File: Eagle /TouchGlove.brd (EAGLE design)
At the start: 69.5 x 25.3 mm, 77 parts, among them Q1 SI2302CDS 2.9A/20V, Q2 SI2302CDS 2.9A/20V, Q3 SI2302CDS 2.9A/20V, Q4 SI2302CDS 2.9A/20V, Q5 SI2302CDS 2.9A/20V, SW1 300mA/4V, Y1 16 MHz

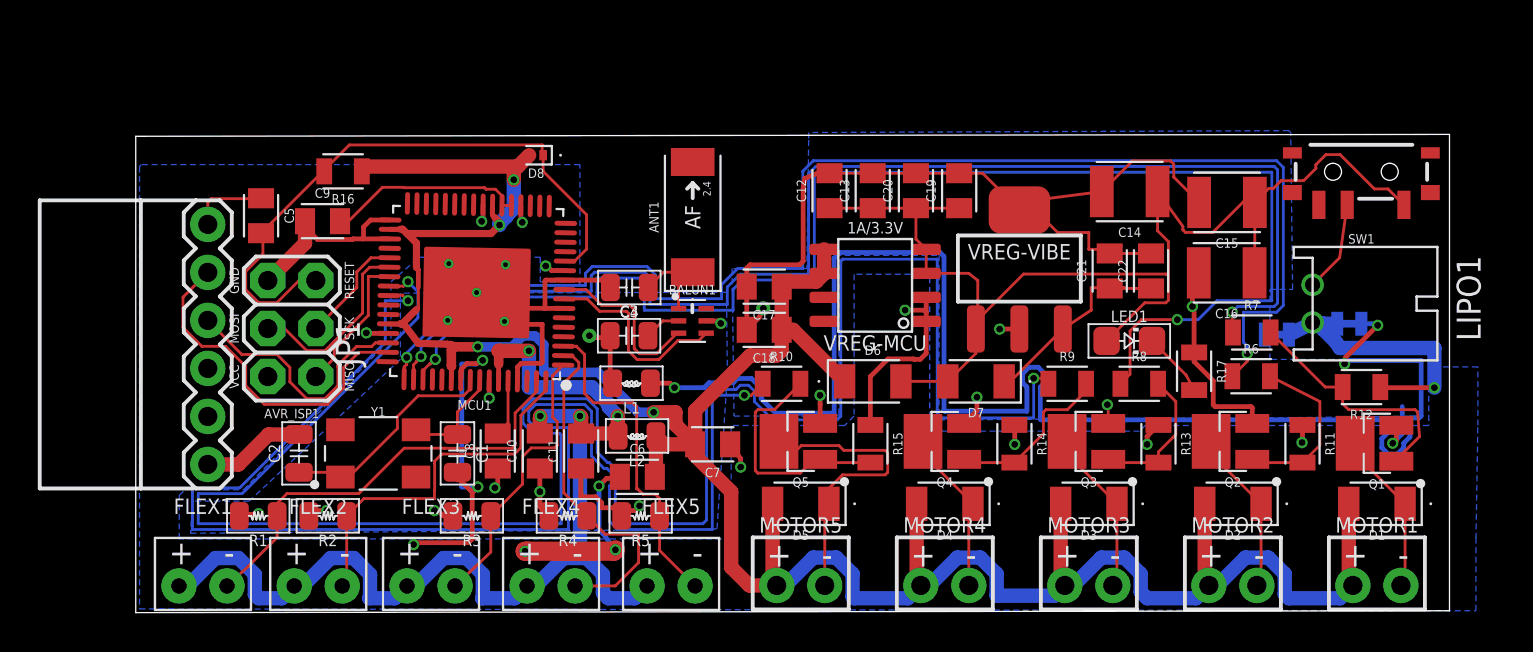
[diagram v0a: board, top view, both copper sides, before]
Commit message: Fixing DRC errors in touchglove brd
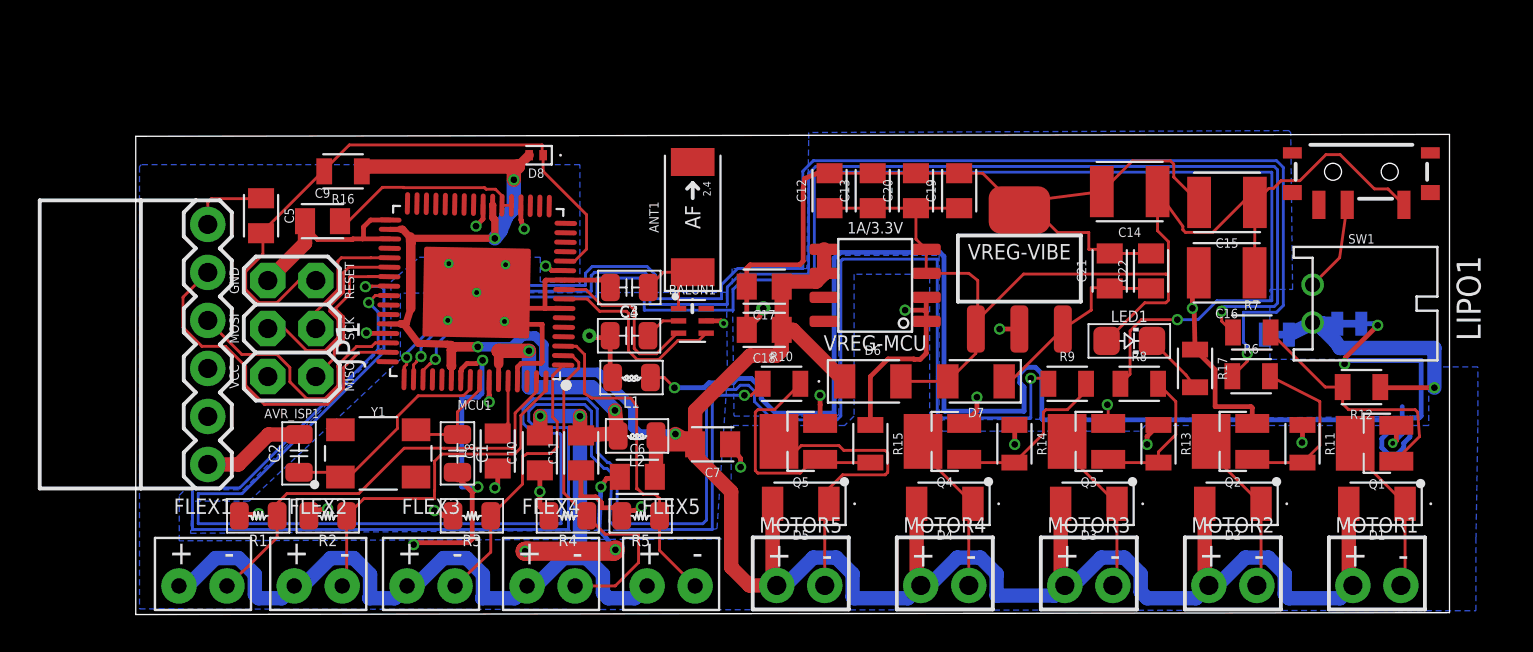
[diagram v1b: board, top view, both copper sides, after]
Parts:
- moved L1 0.30 mm to (34.2, 13.5)
- moved R17 0.16 mm to (64.0, 14.0)
- moved C10 0.10 mm to (29.4, 9.55)
- moved C11 0.10 mm to (31.6, 9.55)
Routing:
- net MISO: track 7.87 -> 9.90 mm
- net VCC: track 144.1 -> 145.4 mm
- net MOSI: track 9.94 -> 10.9 mm
- net PINKY-VIBE: track 73.8 -> 72.8 mm
- net SCK: track 5.93 -> 6.85 mm
- net INDEX-VIBE: track 70.1 -> 71.0 mm
- net AGND: track 37.3 -> 38.2 mm
- net GND: track 77.9 -> 78.6 mm
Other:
- board size 69.5 x 25.3 mm -> 69.5 x 25.4 mm

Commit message: Rotated that shitty chip.
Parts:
- removed D6: 1A/50V, PiB_discrete_semiconductors:SODFL3516X170
- removed MOTOR1, MOTOR2, MOTOR3, MOTOR4, MOTOR5: (no value), PiB:CONNECTOR_MOTOR
- added VIBE1, VIBE2, VIBE3, VIBE4, VIBE5: Molex VERT 1.25mm pitch, PiB_actuators:_MOLEX-0530470210_VERT_PITCH-1.25MM
- FLEX1, FLEX2, FLEX3, FLEX4, FLEX5: device PiB:CONNECTOR_FSR -> PiB_sensors:_MOLEX-0530470210_VERT_PITCH-1.25MM
- VREG-MCU: device PiB_ic_power:SOIC-8_W3.9MM -> PiB_ic_power:SOIC127P600X265-8
- moved D8 14.6 mm to (14.6, 24.6)
- moved SUPPLY39 3.77 mm to (70.0, 13.3), turned to 270 degrees
- moved SUPPLY38 3.16 mm to (68.0, 12.7), turned to 90 degrees
- moved R16 1.23 mm to (17.8, 24.0)
- moved FLEX2 1.20 mm to (17.7, 2.58)
- moved FLEX3 1.20 mm to (23.6, 2.58)
- moved FLEX4 1.20 mm to (30.0, 2.58)
- moved FLEX5 1.20 mm to (36.3, 2.58)
- moved FLEX1 1.15 mm to (11.6, 2.63)
- moved D1 0.76 mm to (73.6, 6.11)
- moved D2 0.75 mm to (66.1, 6.11)
- moved D3 0.75 mm to (58.4, 6.11)
- moved D4 0.75 mm to (50.8, 6.11)
- moved D5 0.75 mm to (43.2, 6.11)
- turned MCU1 to 180 degrees
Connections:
- net AVCC: now also FLEX1.1, FLEX2.1, FLEX3.1, FLEX4.1, FLEX5.1; no longer FLEX1.+, FLEX2.+, FLEX3.+, FLEX4.+, FLEX5.+
- net FLEX-INDEX: now also FLEX2.2; no longer FLEX2.-
- net FLEX-MIDDLE: now also FLEX3.2; no longer FLEX3.-
- net FLEX-PINKY: now also FLEX5.2; no longer FLEX5.-
- net FLEX-RING: now also FLEX4.2; no longer FLEX4.-
- net FLEX-THUMB: now also FLEX1.2; no longer FLEX1.-
- net GND: now also C12.2, C13.2, C14.2, C15.2, C16.2, C17.2, C18.2, R17.1
- net N$1: now also VIBE1.2; no longer MOTOR1.-
- net N$2: now also VIBE2.2; no longer MOTOR2.-
- net N$24: no longer D6.K
- net N$3: now also VIBE3.2; no longer MOTOR3.-
- net N$4: now also VIBE4.2; no longer MOTOR4.-
- net N$5: now also VIBE5.2; no longer MOTOR5.-
- net NGND: no longer C12.2, C13.2, C14.2, C15.2, C16.2, C17.2, C18.2, R17.1
- net VCC: now also VIBE1.1, VIBE2.1, VIBE3.1, VIBE4.1, VIBE5.1; no longer D6.A, MOTOR1.+, MOTOR2.+, MOTOR3.+, MOTOR4.+, MOTOR5.+
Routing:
- net NGND: track 65.4 -> 19.6 mm, vias 7 -> 13
- net N$19: track 78.8 -> 54.4 mm, vias 3 -> 1
- net GND: track 78.6 -> 66.7 mm, vias 16 -> 25
- net VCC: track 145.4 -> 135.1 mm
- net N$5: track 16.5 -> 11.5 mm
- net RING-VIBE: track 107.7 -> 102.9 mm
- net FLEX-RING: track 18.4 -> 14.9 mm
- net RESET: track 32.7 -> 36.1 mm
- net AVCC: track 60.5 -> 57.3 mm, vias 4 -> 5
- net N$22: track 12.8 -> 9.65 mm
- net N$16: track 13.3 -> 16.3 mm
- net N$24: track 64.1 -> 61.9 mm
- net MISO: track 9.90 -> 7.85 mm
- net N$14: track 9.30 -> 10.8 mm
- net N$4: track 8.80 -> 10.3 mm
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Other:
- board size 69.5 x 25.4 mm -> 69.5 x 25.3 mm

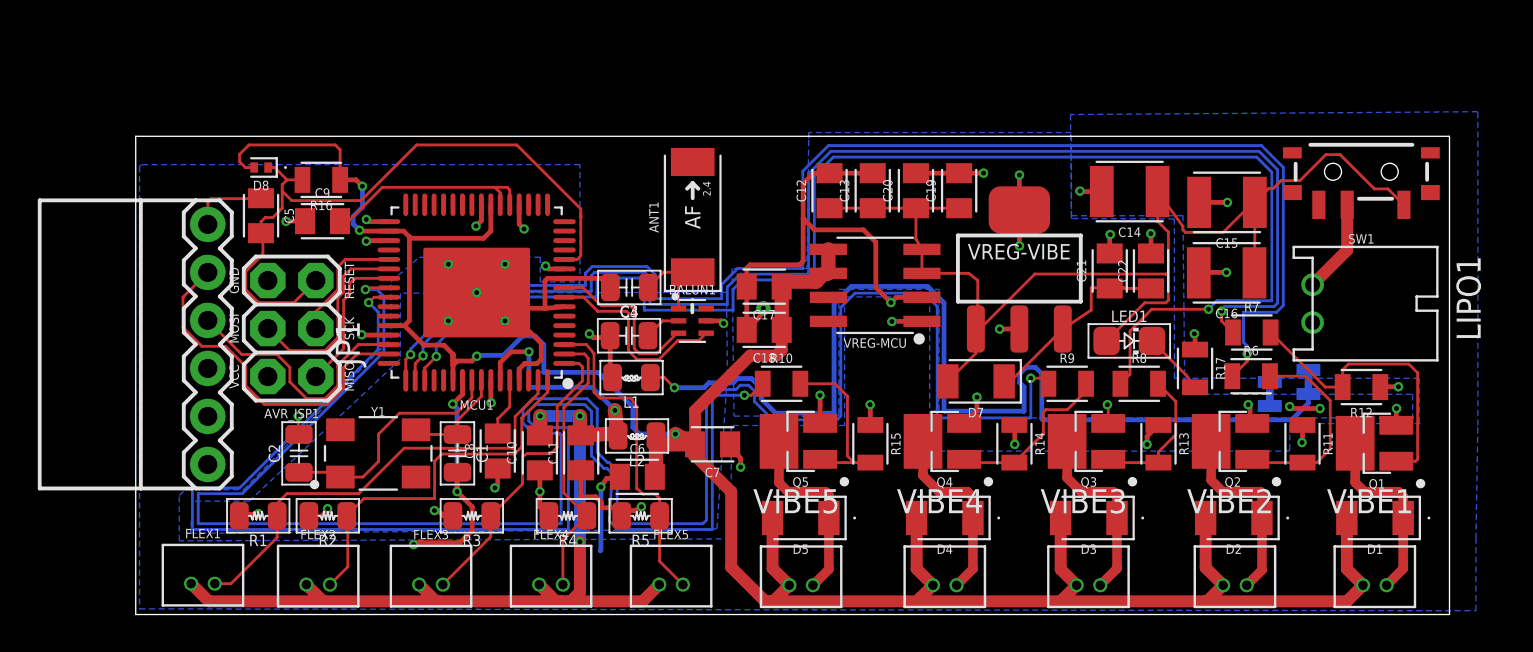
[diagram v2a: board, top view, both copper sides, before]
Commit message: Fixing very large amount of bugs in touch glove schematic
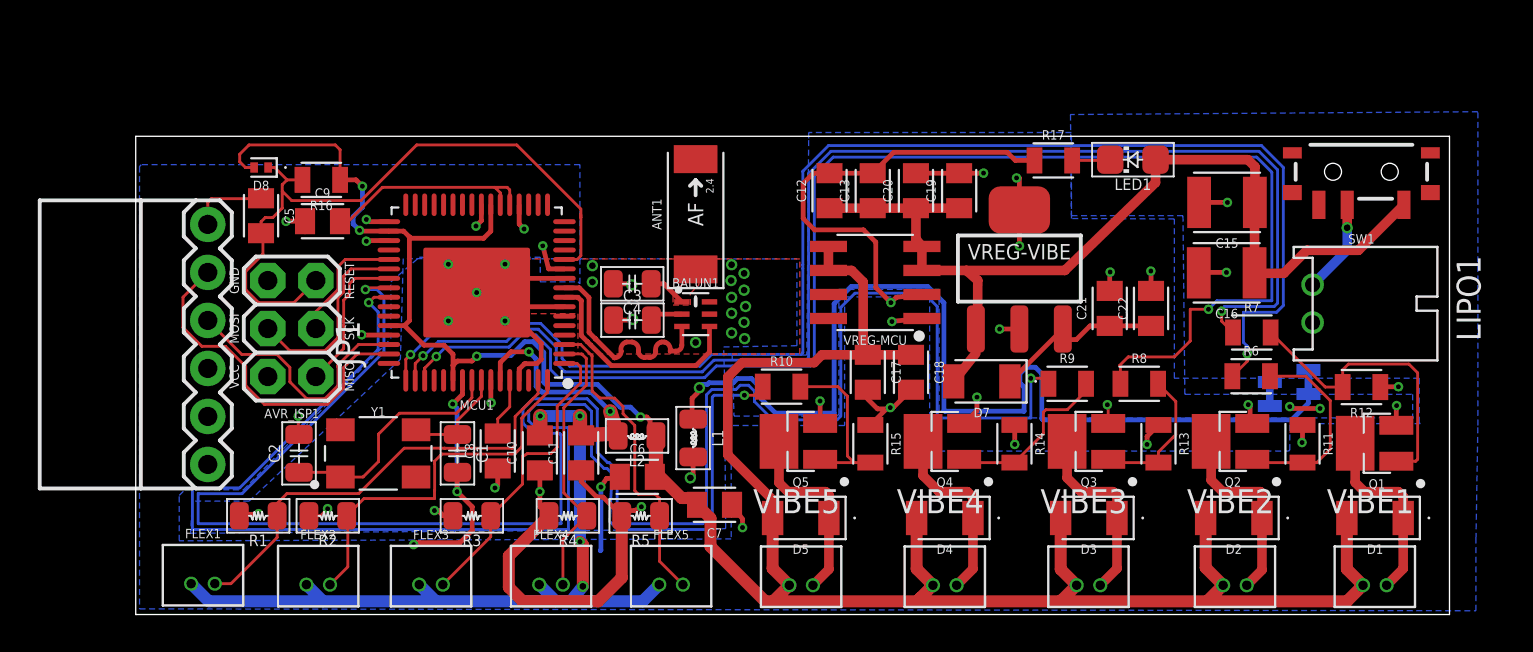
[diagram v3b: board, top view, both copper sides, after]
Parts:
- removed C14: 100uF/10V, PiB_capacitors:CAPC3225X270_SMD-1210
- moved R17 13.3 mm to (56.5, 25.0), turned to 0 degrees
- moved LED1 9.59 mm to (60.8, 25.1), turned to 180 degrees
- moved C18 8.08 mm to (49.0, 13.8), turned to 270 degrees
- moved C17 7.11 mm to (46.7, 13.8), turned to 270 degrees
- moved L1 4.57 mm to (37.5, 10.3), turned to 270 degrees
- moved C7 3.20 mm to (38.6, 6.80)
- moved C21 1.98 mm to (59.5, 17.2)
- moved C22 1.98 mm to (61.7, 17.2)
- moved C3 0.85 mm to (34.3, 16.6)
- moved BALUN1 0.40 mm to (37.6, 16.9)
- moved D7 0.30 mm to (52.8, 13.3)
- moved C4 0.25 mm to (34.3, 18.5)
- moved ANT1 0.22 mm to (37.6, 22.2)
- moved R10 0.15 mm to (42.2, 13.1)
- moved VREG-MCU 0.15 mm to (47.1, 18.6)
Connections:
- removed net N$24: C12.1, C13.1, C14.1, C15.1, C16.1, C19.1, C20.1, D7.K, LED1.A, SW1.1, VREG-MCU.3, VREG-MCU.4, VREG-VIBE.1
- new net VBAT: C12.1, C13.1, C15.1, C16.1, C19.1, C20.1, D7.K, LED1.A, SW1.1, VREG-MCU.3, VREG-MCU.4, VREG-VIBE.1
- net GND: no longer C14.2
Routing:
- net N$24: track 61.9 -> 0.00 mm
- net VBAT: track 0.00 -> 54.6 mm
- net AGND: track 37.8 -> 46.3 mm, vias 9 -> 23
- net VCC: track 135.1 -> 139.8 mm
- net N$9: track 4.92 -> 2.02 mm
- net 3.3V: track 11.9 -> 9.23 mm
- net N$10: track 9.13 -> 11.5 mm
- net GND: track 66.7 -> 68.3 mm, vias 25 -> 22
- net N$25: track 3.35 -> 2.03 mm
- net N$11: track 10.6 -> 11.9 mm
- net N$19: track 54.4 -> 53.4 mm
- net AVCC: track 57.3 -> 56.4 mm, vias 5 -> 6
- net FLEX-PINKY: track 17.3 -> 16.8 mm
- net N$15: vias 0 -> 1
- added copper zone on layer 1, net AGND
- added copper zone on layer 1, net N$9

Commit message: Rev 1: Ready for fab.
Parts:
- added U$1: (no value), PiB_logo:PIB_LOGO_10MM
- C1, C2: device PiB_capacitors:_CER_SMD-805 -> PiB_capacitors:CAPC2012X95_SMD-0805
- C3: value 22PF/250V -> 22pF/250V; device PiB_capacitors:_CER_SMD-805 -> PiB_capacitors:CAPC2012X95_SMD-0805
- C4: value 0.75PF/100V -> 0.75pF/100V; device PiB_capacitors:_CER_SMD-805 -> PiB_capacitors:CAPC2012X95_SMD-0805
- L1, L2: device PiB_inductors:_SMD-805 -> PiB_inductors:INDC2012X145
- LED1: device PiB_leds:LED_SMD-805_ -> PiB_leds:LEDC2012X120_LED-0805
- R1, R2, R3, R4, R5: device PiB_resistors:RESISTOR_SMD-805 -> PiB_resistors:RESC2012X60_SMD-0805
- VREG-VIBE: device PiB_ic_power:SOT223-4 -> PiB_ic_power:SOT229P700X180-4
- moved C7 0.30 mm to (38.3, 6.80)
- moved R13 0.25 mm to (61.8, 10.0)
- moved C1 0.13 mm to (25.0, 9.65)
- turned VREG-VIBE to 90 degrees
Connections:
- net 3.3V: now also D1.K, D2.K, D3.K, D4.K, D5.K, VIBE1.1, VIBE2.1, VIBE3.1, VIBE4.1, VIBE5.1
- net NGND: now also VREG-VIBE.4; no longer VREG-VIBE.TAB
- net VCC: no longer D1.K, D2.K, D3.K, D4.K, D5.K, VIBE1.1, VIBE2.1, VIBE3.1, VIBE4.1, VIBE5.1
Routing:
- net 3.3V: track 9.23 -> 83.2 mm
- net VCC: track 139.8 -> 75.6 mm
- net GND: track 68.3 -> 79.6 mm
- net AGND: track 46.3 -> 41.2 mm, vias 23 -> 21
- net NGND: track 19.4 -> 18.1 mm
- net N$5: track 11.5 -> 10.2 mm
- net VBAT: track 54.6 -> 53.4 mm
- net N$22: track 9.59 -> 9.09 mm
- net MIDDLE-VIBE: track 76.9 -> 77.1 mm, vias 2 -> 4
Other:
- board text added: "CADed by: Odeh Saba"
- board text added: "Rev 1"
- board text added: "Transmission of Touch"
